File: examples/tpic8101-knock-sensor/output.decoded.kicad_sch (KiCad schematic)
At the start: 21 parts, among them IC19 TPIC8101DWRG4, Y1 S35010-4.000-A-X1-R

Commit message: Add footprint lookup table for TOKN decoder
- Add footprints.json with comprehensive lookup table:
  - Common passive sizes (0402, 0603, 0805, etc.)
  - IC packages (SOIC, TSSOP, QFN, LQFP, etc.)
  - Specific parts (MCP2551, MAX232, ATmega, STM32, etc.)
  - Transistors, regulators, op-amps, and more

- Update tokn_decoder.py to auto-populate footprints:
  - Priority: explicit > package hint > part match > passive type
  - Handles size codes (0603) for passives automatically

Decoded schematics now have proper footprints ready for PCB layout.
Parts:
- C82, C83, C84, C85, C86, C87, C88, C89: footprint (none) -> Capacitor_SMD:C_0603_1608Metric
- IC19: footprint SOIC-127 -> Package_SO:SOIC-20W_7.5x12.8mm_P1.27mm
- R83, R84, R85, R86, R87, R88, R89, R90, R91, R92, R93: footprint 0603 -> Resistor_SMD:R_0603_1608Metric
- Y1: footprint S350104000AX1R -> (none)
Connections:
- net +5VD: now also IC19.1, Y1.4
- net 5V-KNOCK: now also IC19.4; no longer IC19.2
- net GND: now also IC19.2, Y1.2; no longer IC19.4, Y1.3
- net KNOCK-INTN-HOLD: now also IC19.7; no longer IC19.8
- net SPI-KNOCK-CS: now also IC19.8; no longer IC19.7
- net SPI-MISO: now also IC19.11; no longer IC19.9
- net SPI-MOSI: now also IC19.12
- net SPI-SCLK: now also IC19.13
- net at R83.1, R84.2: now also IC19.19
- net at IC19.15, IC19.20, IC19.3: now also C86.2
- net at IC19.16: now also R85.2, R86.1
- net at IC19.17: now also R86.2
- net at IC19.18: now also R83.2
- new net: C88.1, IC19.9, Y1.3
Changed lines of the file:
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@@
       (at 91.44 55.8 0)
       (effects (font (size 1.27 1.27))))
-    (property "Footprint" ""
+    (property "Footprint" "Capacitor_SMD:C_0603_1608Metric"
       (at 91.44 50.8 0)
       (effects (font (size 1.27 1.27)) (hide yes)))
@@
       (at 78.74 55.8 0)
       (effects (font (size 1.27 1.27))))
-    (property "Footprint" ""
+    (property "Footprint" "Capacitor_SMD:C_0603_1608Metric"
       (at 78.74 50.8 0)
       (effects (font (size 1.27 1.27)) (hide yes)))
@@
       (at 69.85 88.82 0)
       (effects (font (size 1.27 1.27))))
-    (property "Footprint" ""
+    (property "Footprint" "Capacitor_SMD:C_0603_1608Metric"
       (at 69.85 83.82 0)
       (effects (font (size 1.27 1.27)) (hide yes)))
@@
       (at 69.85 105.33 0)
       (effects (font (size 1.27 1.27))))
-    (property "Footprint" ""
+    (property "Footprint" "Capacitor_SMD:C_0603_1608Metric"
       (at 69.85 100.33 0)
       (effects (font (size 1.27 1.27)) (hide yes)))
@@
       (at 99.06 98.98 0)
       (effects (font (size 1.27 1.27))))
-    (property "Footprint" ""
+    (property "Footprint" "Capacitor_SMD:C_0603_1608Metric"
       (at 99.06 93.98 0)
       (effects (font (size 1.27 1.27)) (hide yes)))
@@
       (at 114.3 140.89 0)
       (effects (font (size 1.27 1.27))))
-    (property "Footprint" ""
+    (property "Footprint" "Capacitor_SMD:C_0603_1608Metric"
       (at 114.3 135.89 0)
       (effects (font (size 1.27 1.27)) (hide yes)))
@@
       (at 166.37 139.62 0)
       (effects (font (size 1.27 1.27))))
-    (property "Footprint" ""
+    (property "Footprint" "Capacitor_SMD:C_0603_1608Metric"
       (at 166.37 134.62 0)
       (effects (font (size 1.27 1.27)) (hide yes)))
@@
       (at 213.36 121.84 0)
       (effects (font (size 1.27 1.27))))
-    (property "Footprint" ""
+    (property "Footprint" "Capacitor_SMD:C_0603_1608Metric"
       (at 213.36 116.84 0)
       (effects (font (size 1.27 1.27)) (hide yes)))
@@
       (at 135.89 100.25 0)
       (effects (font (size 1.27 1.27))))
-    (property "Footprint" "SOIC-127"
+    (property "Footprint" "Package_SO:SOIC-20W_7.5x12.8mm_P1.27mm"
       (at 135.89 95.25 0)
       (effects (font (size 1.27 1.27)) (hide yes)))
@@
       (at 100.33 86.28 0)
       (effects (font (size 1.27 1.27))))
-    (property "Footprint" "0603"
+    (property "Footprint" "Resistor_SMD:R_0603_1608Metric"
       (at 100.33 81.28 0)
       (effects (font (size 1.27 1.27)) (hide yes)))
@@
       (at 85.09 88.82 0)
       (effects (font (size 1.27 1.27))))
-    (property "Footprint" "0603"
+    (property "Footprint" "Resistor_SMD:R_0603_1608Metric"
       (at 85.09 83.82 0)
       (effects (font (size 1.27 1.27)) (hide yes)))
@@
       (at 85.09 105.33 0)
       (effects (font (size 1.27 1.27))))
-    (property "Footprint" "0603"
+    (property "Footprint" "Resistor_SMD:R_0603_1608Metric"
       (at 85.09 100.33 0)
       (effects (font (size 1.27 1.27)) (hide yes)))
@@
       (at 99.06 107.87 0)
       (effects (font (size 1.27 1.27))))
-    (property "Footprint" "0603"
+    (property "Footprint" "Resistor_SMD:R_0603_1608Metric"
       (at 99.06 102.87 0)
       (effects (font (size 1.27 1.27)) (hide yes)))
@@
       (at 179.07 112.95 0)
       (effects (font (size 1.27 1.27))))
-    (property "Footprint" "0603"
+    (property "Footprint" "Resistor_SMD:R_0603_1608Metric"
       (at 179.07 107.95 0)
       (effects (font (size 1.27 1.27)) (hide yes)))
@@
       (at 185.42 112.95 0)
       (effects (font (size 1.27 1.27))))
-    (property "Footprint" "0603"
+    (property "Footprint" "Resistor_SMD:R_0603_1608Metric"
       (at 185.42 107.95 0)
       (effects (font (size 1.27 1.27)) (hide yes)))
@@
       (at 191.77 112.95 0)
       (effects (font (size 1.27 1.27))))
-    (property "Footprint" "0603"
+    (property "Footprint" "Resistor_SMD:R_0603_1608Metric"
       (at 191.77 107.95 0)
       (effects (font (size 1.27 1.27)) (hide yes)))
@@
       (at 198.12 112.95 0)
       (effects (font (size 1.27 1.27))))
-    (property "Footprint" "0603"
+    (property "Footprint" "Resistor_SMD:R_0603_1608Metric"
       (at 198.12 107.95 0)
       (effects (font (size 1.27 1.27)) (hide yes)))
@@
       (at 204.47 112.95 0)
       (effects (font (size 1.27 1.27))))
-    (property "Footprint" "0603"
+    (property "Footprint" "Resistor_SMD:R_0603_1608Metric"
       (at 204.47 107.95 0)
       (effects (font (size 1.27 1.27)) (hide yes)))
@@
       (at 210.82 112.95 0)
       (effects (font (size 1.27 1.27))))
-    (property "Footprint" "0603"
+    (property "Footprint" "Resistor_SMD:R_0603_1608Metric"
       (at 210.82 107.95 0)
       (effects (font (size 1.27 1.27)) (hide yes)))
@@
       (at 172.72 112.95 0)
       (effects (font (size 1.27 1.27))))
-    (property "Footprint" "0603"
+    (property "Footprint" "Resistor_SMD:R_0603_1608Metric"
       (at 172.72 107.95 0)
       (effects (font (size 1.27 1.27)) (hide yes)))
@@
       (at 137.16 135.81 0)
       (effects (font (size 1.27 1.27))))
-    (property "Footprint" "S350104000AX1R"
+    (property "Footprint" ""
       (at 137.16 130.81 0)
       (effects (font (size 1.27 1.27)) (hide yes)))

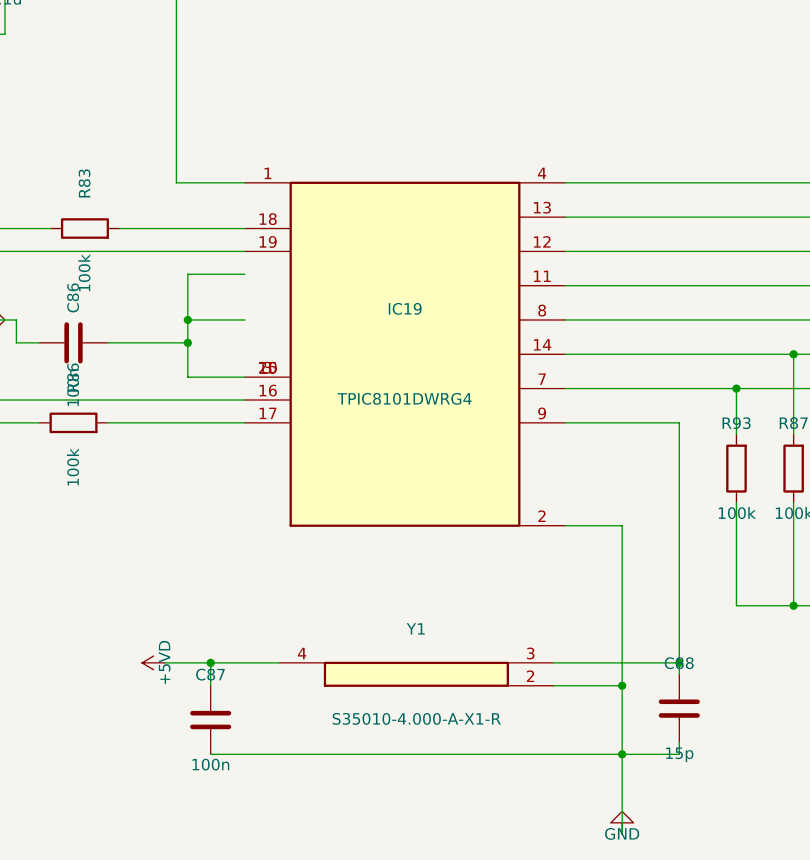
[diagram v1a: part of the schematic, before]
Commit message: Fix decoder pin placement using TOKN pins section
- Use pin definitions from TOKN pins{REF}[N]: section instead of
  deriving positions from wire endpoints
- Calculate pin positions using standard dual-inline IC layout:
  pins 1-N/2 on left (top to bottom), N/2+1 to N on right (bottom to top)
- Include pin names from TOKN in generated lib_symbols
- Fix issue where pins with same net were merged to same position
- Regenerate all decoded schematics with correct pin placement
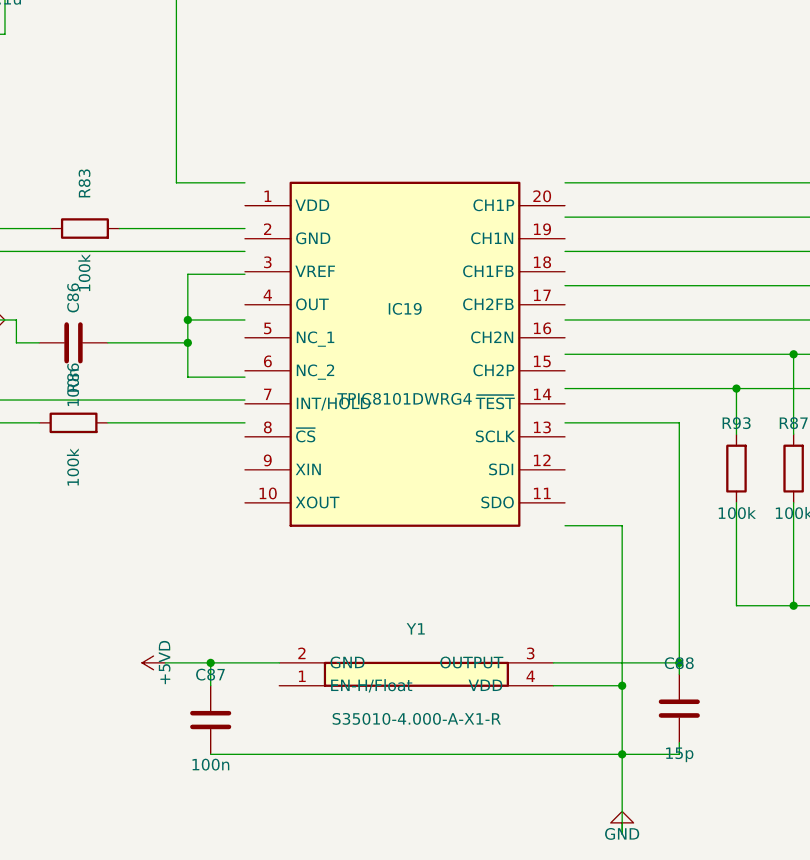
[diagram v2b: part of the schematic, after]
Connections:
- net +5VD: now also Y1.2 (GND); no longer IC19.1, Y1.4
- net 5V-KNOCK: no longer IC19.4
- net GND: now also Y1.4 (VDD); no longer IC19.2, Y1.2
- net KNOCK-INTN-HOLD: no longer IC19.7
- net KNOCK-TESTN: no longer IC19.14
- net SPI-KNOCK-CS: no longer IC19.8
- net SPI-MISO: no longer IC19.11
- net SPI-MOSI: no longer IC19.12
- net SPI-SCLK: no longer IC19.13
- net at R83.1, R84.2: no longer IC19.19
- net at R85.2, R86.1: no longer IC19.16
- net at IC19.17 (CH2FB): no longer R86.2
- net at IC19.18 (CH1FB): no longer R83.2
- net at C88.1, Y1.3 (OUTPUT): no longer IC19.9
- now unconnected: C86.2, IC19.15, IC19.20, IC19.3
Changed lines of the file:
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@@
     (pin "2"
+    )
+    (pin "3"
     )
     (pin "4"
     )
+    (pin "5"
+    )
+    (pin "6"
+    )
     (pin "7"
     )
+    (pin "8"
+    )
+    (pin "9"
+    )
+    (pin "10"
+    )
+    (pin "11"
+    )
+    (pin "12"
+    )
+    (pin "13"
+    )
     (pin "14"
     )
-    (pin "8"
-    )
-    (pin "11"
-    )
-    (pin "12"
-    )
-    (pin "13"
-    )
-    (pin "3"
-    )
     (pin "15"
     )
+    (pin "16"
+    )
+    (pin "17"
+    )
+    (pin "18"
+    )
+    (pin "19"
+    )
     (pin "20"
-    )
-    (pin "17"
-    )
-    (pin "16"
-    )
-    (pin "19"
-    )
-    (pin "9"
-    )
-    (pin "18"
     )
     (instances
@@
       (at 137.16 130.81 0)
       (effects (font (size 1.27 1.27)) (hide yes)))
+    (pin "1"
+    )
+    (pin "2"
+    )
+    (pin "3"
+    )
     (pin "4"
     )
-    (pin "2"
-    )
-    (pin "3"
-    )
-    (instances
+    (instances
